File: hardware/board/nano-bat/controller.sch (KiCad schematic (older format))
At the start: 24 parts

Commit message: Adding larger microcontroller
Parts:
- removed U?: STM32L452CEUx, Package_DFN_QFN:QFN-48-1EP_7x7mm_P0.5mm_EP5.6x5.6mm, symbol MCU_ST_STM32L4:STM32L452CEUx
- added C?: .1u, symbol Device:C
- added D?: LED, symbol Device:LED
- added J?: Conn_01x10, symbol Connector_Generic:Conn_01x10
- added R?: R_US, symbol Device:R_US
- added R?: 1k, symbol Device:R_US
- added R? (x2): 10k, symbol Device:R_US
- added SW?: SW_Push, symbol Switch:SW_Push
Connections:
- net labels added: BTN1, BTN2, BTN3, BTN4, PB5, PD2, SPI2_MISO, SPI2_MOSI, SPI2_NSS, SPI2_SCK, SWCLK
- net labels removed: SWDCLK
- wire segments 191 -> 219
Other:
- moved on the sheet: C?, FB?, J?, R?, SW?, U?

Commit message: Adding WIP before reverting
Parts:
- removed U?: STM32L452RETx, Package_QFP:LQFP-64_10x10mm_P0.5mm, symbol MCU_ST_STM32L4:STM32L452RETx
- added U?: STM32L452CEUx, Package_DFN_QFN:QFN-48-1EP_7x7mm_P0.5mm_EP5.6x5.6mm, symbol MCU_ST_STM32L4:STM32L452CEUx
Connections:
- net labels added: CC_SCL, CC_SDA, CC_~AL~CC, TFT_BL_CNTRL
- net labels removed: CC_POL, CC_~INT, CC_~SHDN, DB0, DB1, DB2, DB3, DB4, DB5, DB6, DB7, LCD-TFT_DB, LCD_EN, LCD_RS, LCD_R~W, TFT_RD, TFT_RGB_DOTCLK, TFT_RGB_EN, TFT_RGB_HSYNC, TFT_RGB_VSYNC, TFT_WR
- wire segments 219 -> 192
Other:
- moved on the sheet: C?, FB?, R?

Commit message: Adding complete schematic
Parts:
- removed R? (x2): 10k, symbol Device:R_US
- added D?: LED, symbol Device:LED
- added R?: 1k, symbol Device:R_US
- R? (x5): value R_US -> 10k
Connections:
- net labels added: +2V8, I2C1_SCL, I2C1_SDA, PA2, PA8, TFT_D~CX
- net labels removed: +3.3V, PB5, PD2, Vsoc
- wire segments 192 -> 203
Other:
- moved on the sheet: C?, D?, FB?, J?, R?, SW?, U?

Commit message: Adding first-pass revisions and annotations, part selection
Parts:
- removed C? (x5): .1u, symbol Device:C
- removed C?: 4.7u, symbol Device:C
- removed C?: 1u, symbol Device:C
- removed FB?: Ferrite_Bead_Small, symbol Device:Ferrite_Bead_Small
- removed J?: Conn_01x10, symbol Connector_Generic:Conn_01x10
- removed R? (x7): 10k, symbol Device:R_US
- removed R? (x2): 1k, symbol Device:R_US
- removed SW? (x3): SW_Push, symbol Switch:SW_Push
- added C301, C302, C303, C304, C305, C308, C309, C310, C311: 0.1u, Capacitor_SMD:C_0603_1608Metric, symbol Device:C
- added C307: 1u, Capacitor_SMD:C_0603_1608Metric, symbol Device:C
- added C312: 4.7u, Capacitor_SMD:C_0603_1608Metric, symbol Device:C
- added FB302: Ferrite_Bead_Small, Resistor_SMD:R_0603_1608Metric, symbol Device:Ferrite_Bead_Small
- added J303: Conn_01x10, Connector_PinHeader_2.54mm:PinHeader_1x10_P2.54mm_Vertical, symbol Connector_Generic:Conn_01x10
- added R302, R304, R306, R308, R309, R311: 1k, Resistor_SMD:R_0603_1608Metric, symbol Device:R_US
- added R303, R305, R307, R310, R312, R313, R314: 10k, Resistor_SMD:R_0603_1608Metric, symbol Device:R_US
- added SW302, SW303, SW304: SW_Push, footprints:SW_B3FS-1010P, symbol Switch:SW_Push
- C306: renamed from C?; footprint (none) -> Capacitor_SMD:C_0603_1608Metric; Part (none) -> 399-7842-1-ND
- D301: renamed from D?; value LED -> BLU; footprint (none) -> LED_SMD:LED_0805_2012Metric; Part (none) -> 160-1645-1-ND
- D302: renamed from D?; value LED -> RED; footprint (none) -> LED_SMD:LED_0805_2012Metric; Part (none) -> 475-1278-1-ND
- FB301: renamed from FB?; footprint (none) -> Resistor_SMD:R_0603_1608Metric; Part (none) -> 587-1923-1-ND
- J301: renamed from J?; footprint (none) -> Connector_PinHeader_1.27mm:PinHeader_2x05_P1.27mm_Vertical_SMD; Part (none) -> SAM8796-ND
- J302: renamed from J?; footprint (none) -> Connector_PinHeader_2.54mm:PinHeader_1x10_P2.54mm_Vertical; Part (none) -> 609-3301-ND
- R301: renamed from R?; footprint (none) -> Resistor_SMD:R_0603_1608Metric; Part (none) -> 311-10KGRCT-ND
- SW301: renamed from SW?; footprint (none) -> footprints:SW_B3FS-1010P; Part (none) -> SW1440CT-ND
- U301: renamed from U?; Part (none) -> 497-6357-5-ND
- U302: renamed from U?; Part (none) -> 497-17218-ND
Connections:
- net +2V8: now also C308.1, C309.1, C310.1, C311.1, C312.1, FB302.2, J303.2 (Pin_2), J303.9 (Pin_9), R303.1, R305.1, R307.1, R309.1, R310.1, R311.1, R312.1, R313.1, R314.1
- net BTN1: now also C301.1, R302.1; no longer SW301.1
- net BTN2: now also C302.1, R303.2, R304.1
- net BTN3: now also C303.1, R305.2, R306.1
- net BTN4: now also C304.1, R307.2, R308.1
- net GND: now also C301.2, C302.2, C303.2, C304.2, C305.1, C308.2, C309.2, C310.2, C311.2, C312.2, J303.1 (Pin_1), J303.10 (Pin_10), SW302.2, SW303.2, SW304.2
- net GNDREF: now also C307.2
- net PA8: now also J303.3 (Pin_3)
- net SPI1_NSS: now also R313.2
- net TFT_MISO: now also J303.6 (Pin_6), J303.7 (Pin_7)
- net TFT_SCK: now also J303.5 (Pin_5)
- net TFT_~CS: now also J303.8 (Pin_8)
- net VDDA: now also C307.1, FB302.1
- net ~RST: now also C305.2, R314.2
- net at U301.3 (~W): now also R310.2
- net at U301.7 (~HOLD): now also R312.2
- net PB8: now reaches U302.45 (PB8)
- net PB8: now also J303.4 (Pin_4)
- net at D302.2 (A): now also R311.2
- net at D301.2 (A): now also R309.2
- net PA2 renamed Pen
- new net: R302.2, SW301.1
- new net: R304.2, SW302.1
- new net: R306.2, SW303.1
- new net: R308.2, SW304.1
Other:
- moved on the sheet: D301, D302, R301, SW301, U301, U302

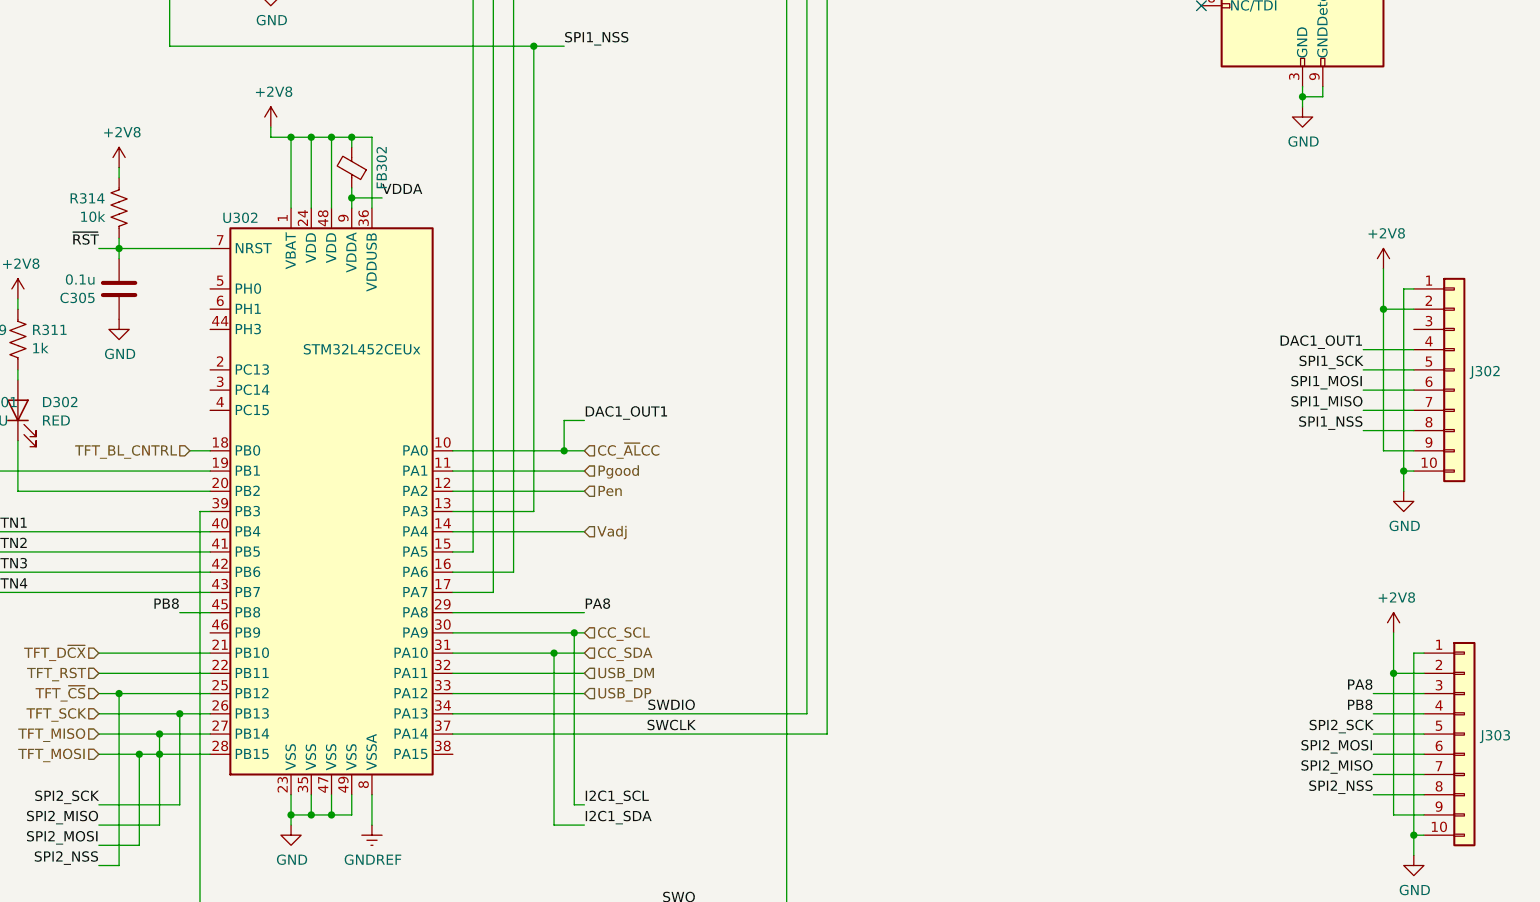
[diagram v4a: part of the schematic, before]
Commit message: Adding 3D models, reorg, minor schematic fixes
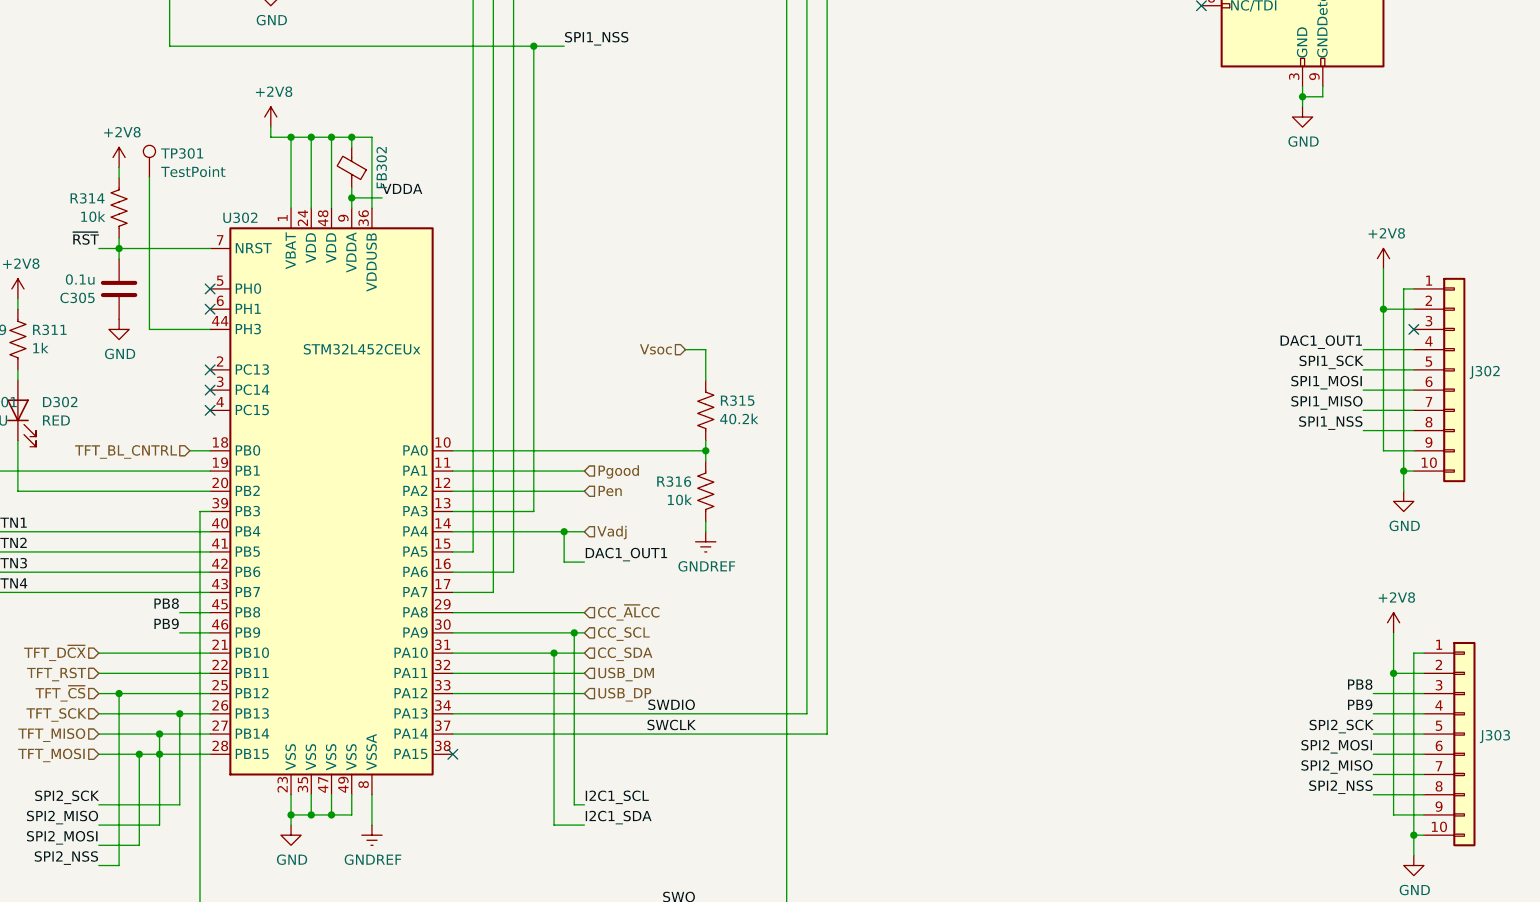
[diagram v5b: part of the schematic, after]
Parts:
- added R315: 40.2k, Resistor_SMD:R_0603_1608Metric, symbol Device:R_US
- added R316: 10k, Resistor_SMD:R_0603_1608Metric, symbol Device:R_US
- added TP301: TestPoint, TestPoint:TestPoint_Plated_Hole_D2.0mm, symbol Connector:TestPoint
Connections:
- net CC_~AL~CC: now also U302.29 (PA8); no longer J302.4 (Pin_4), U302.10 (PA0)
- net GNDREF: now also R316.2
- net PB8: now also J303.3 (Pin_3); no longer J303.4 (Pin_4)
- net Vadj: now also J302.4 (Pin_4)
- net at U302.44 (PH3): now also TP301.1
- net PB9: now reaches U302.46 (PB9)
- net PB9: now also J303.4 (Pin_4)
- removed net PA8: J303.3 (Pin_3), U302.29 (PA8)
- new net: R315.2, R316.1, U302.10 (PA0)
- new net Vsoc: R315.1
- no-connect marks 1 -> 8
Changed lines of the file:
@@
 	9800 2300 9800 2350
 NoConn ~ 9300 1850
-Text HLabel 6250 4450 2    50   Input ~ 0
-Vadj
 Text Label 10100 3550 2    50   ~ 0
 DAC1_OUT1
@@
 Text HLabel 6250 4950 2    50   Input ~ 0
 CC_SCL
-Text HLabel 6250 4050 2    50   Input ~ 0
-CC_~AL~CC
 $Comp
 L MCU_ST_STM32L4:STM32L452CEUx U302
@@
 	6150 1400 5800 1400
 Wire Wire Line
-	5600 4450 6250 4450
+	5600 4450 6150 4450
 Connection ~ 5700 1300
 Connection ~ 5800 1400
@@
 	6150 2050 6000 2050
 Connection ~ 6000 2050
-Wire Wire Line
-	6150 4050 5600 4050
-Wire Wire Line
-	6250 4050 6150 4050
-Connection ~ 6150 4050
-Wire Wire Line
-	6150 3900 6150 4050
-Wire Wire Line
-	6250 3900 6150 3900
-Text Label 6250 3900 0    50   ~ 0
+Text Label 6250 4600 0    50   ~ 0
 DAC1_OUT1
 Text Label 3500 4450 2    50   ~ 0
@@
 Wire Wire Line
 	3150 4000 3150 4150
-Text Label 6250 4850 0    50   ~ 0
-PA8
-Wire Wire Line
-	5600 4850 6250 4850
 Text Label 4250 4850 2    50   ~ 0
 PB8
 Text Label 10150 5250 2    50   ~ 0
-PA8
-Text Label 10150 5350 2    50   ~ 0
 PB8
+Text Label 10150 5350 2    50   ~ 0
+PB9
 Wire Wire Line
 	10150 5350 10400 5350
@@
 	1    0    0    -1
 $EndComp
+Text HLabel 6250 4450 2    50   Input ~ 0
+Vadj
+Text HLabel 6250 4850 2    50   Input ~ 0
+CC_~AL~CC
+Wire Wire Line
+	6250 4600 6150 4600
+Wire Wire Line
+	6150 4600 6150 4450
+Connection ~ 6150 4450
+Wire Wire Line
+	6150 4450 6250 4450
+$Comp
+L Device:R_US R315
+U 1 1 5E695531
+P 6850 3850
+F 0 "R315" H 6918 3896 50  0000 L CNN
+F 1 "40.2k" H 6918 3805 50  0000 L CNN
+F 2 "Resistor_SMD:R_0603_1608Metric" V 6890 3840 50  0001 C CNN
+F 3 "~" H 6850 3850 50  0001 C CNN
+F 4 "RR08P40.2KDCT-ND" H 6850 3850 50  0001 C CNN "Part"
+	1    6850 3850
+	1    0    0    -1
+$EndComp
+Text HLabel 6750 3550 0    50   Input ~ 0
+Vsoc
+$Comp
+L power:GNDREF #PWR0168
+U 1 1 5E6A65E6
+P 6850 4450
+F 0 "#PWR0168" H 6850 4200 50  0001 C CNN
+F 1 "GNDREF" H 6855 4277 50  0000 C CNN
+F 2 "" H 6850 4450 50  0001 C CNN
+F 3 "" H 6850 4450 50  0001 C CNN
+	1    6850 4450
+	1    0    0    -1
+$EndComp
+Wire Wire Line
+	6850 4450 6850 4400
+Wire Wire Line
+	6750 3550 6850 3550
+Wire Wire Line
+	6850 3550 6850 3700
+Wire Wire Line
+	6850 4100 6850 4050
+Wire Wire Line
+	5600 4050 6850 4050
+Connection ~ 6850 4050
+Wire Wire Line
+	6850 4050 6850 4000
+Wire Wire Line
+	6250 4850 5600 4850
+Text Label 4250 4950 2    50   ~ 0
+PB9
+Wire Wire Line
+	4250 4950 4400 4950
+$Comp
+L Device:R_US R316
+U 1 1 5E72ACDB
+P 6850 4250
+F 0 "R316" H 6918 4296 50  0000 L CNN
+F 1 "10k" H 6918 4205 50  0000 L CNN
+F 2 "Resistor_SMD:R_0603_1608Metric" V 6890 4240 50  0001 C CNN
+F 3 "~" H 6850 4250 50  0001 C CNN
+F 4 "311-10KGRCT-ND" H 6850 4250 50  0001 C CNN "Part"
+	1    6850 4250
+	-1   0    0    -1
+$EndComp
+NoConn ~ 10350 3450
+$Comp
+L Connector:TestPoint TP301
+U 1 1 5E73C90B
+P 4100 2700
+F 0 "TP301" H 4158 2818 50  0000 L CNN
+F 1 "TestPoint" H 4158 2727 50  0000 L CNN
+F 2 "TestPoint:TestPoint_Plated_Hole_D2.0mm" H 4300 2700 50  0001 C CNN
+F 3 "~" H 4300 2700 50  0001 C CNN
+	1    4100 2700
+	1    0    0    -1
+$EndComp
+Wire Wire Line
+	4400 3450 4100 3450
+Wire Wire Line
+	4100 3450 4100 2700
+NoConn ~ 5600 5550
+NoConn ~ 4400 3350
+NoConn ~ 4400 3250
+NoConn ~ 4400 3650
+NoConn ~ 4400 3750
+NoConn ~ 4400 3850
 $EndSCHEMATC

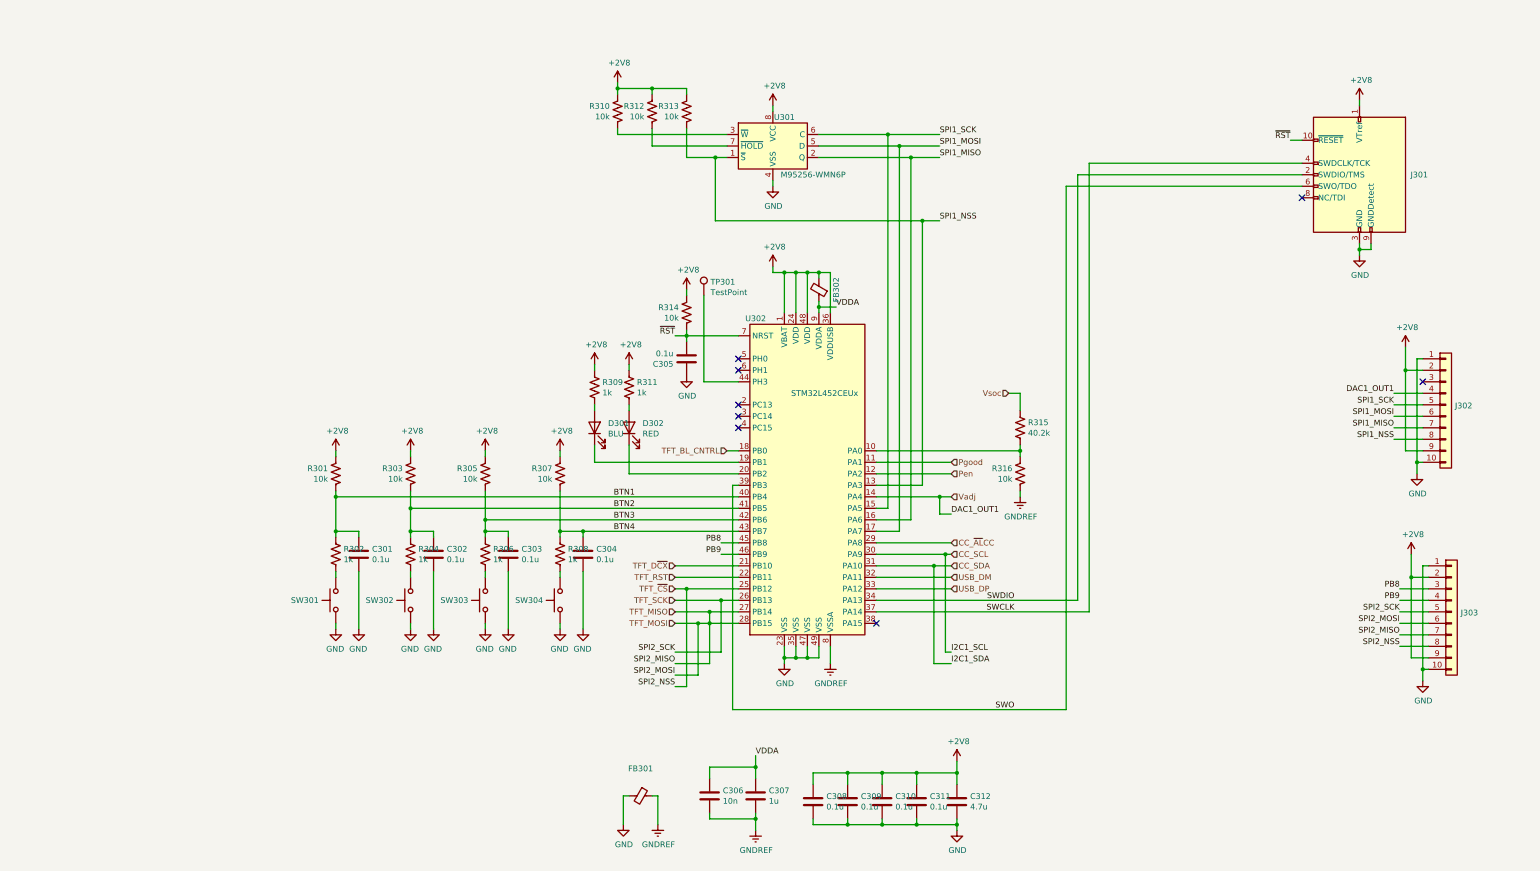
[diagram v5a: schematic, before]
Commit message: Adding docs to schematic
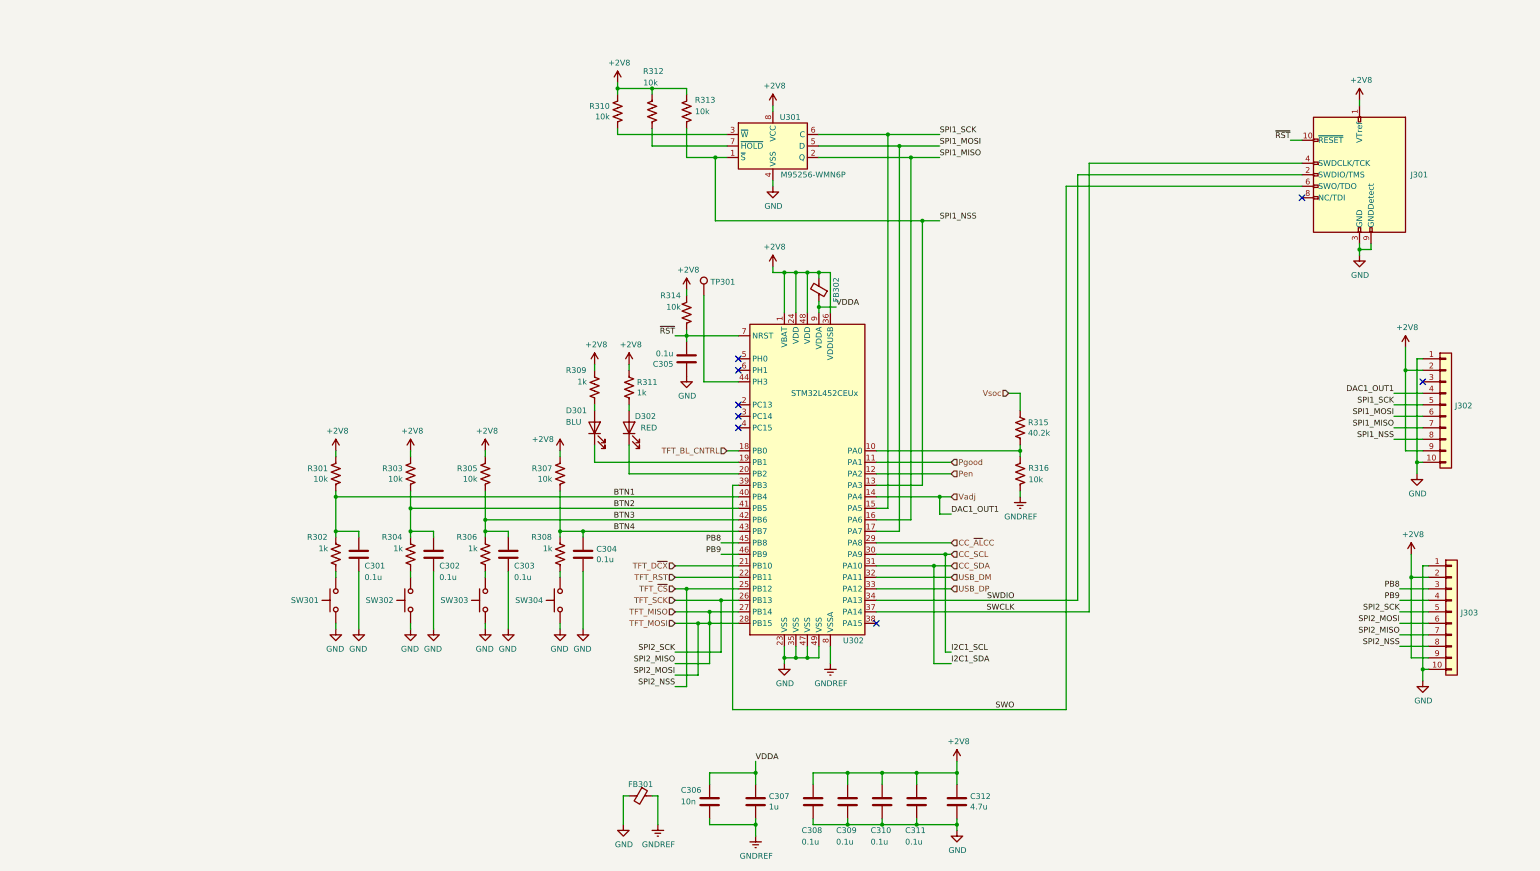
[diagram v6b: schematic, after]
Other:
- moved on the sheet: C306, C307

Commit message: Adding 0.1.0 of board spin
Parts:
- removed D301: BLU, LED_SMD:LED_0805_2012Metric, symbol Device:LED
- removed R309: 1k, Resistor_SMD:R_0603_1608Metric, symbol Device:R_US
- added TP302, TP303, TP304, TP305, TP306: TestPoint, TestPoint:TestPoint_Pad_D1.0mm, symbol Connector:TestPoint
- TP301: footprint TestPoint:TestPoint_Plated_Hole_D2.0mm -> TestPoint:TestPoint_THTPad_D1.0mm_Drill0.5mm
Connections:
- net +2V8: now also J302.3 (Pin_3), J302.4 (Pin_4); no longer J302.2 (Pin_2), J302.9 (Pin_9), J303.2 (Pin_2), J303.9 (Pin_9)
- net BTN1: now also TP302.1
- net BTN2: now also TP303.1
- net BTN3: now also TP304.1
- net BTN4: now also TP305.1
- net CC_SCL: now also J303.9 (Pin_9)
- net CC_SDA: now also J303.8 (Pin_8)
- net CC_~AL~CC: now also TP306.1
- net PB8: now also J302.2 (Pin_2); no longer J303.3 (Pin_3)
- net PB9: now also J303.7 (Pin_7); no longer J303.4 (Pin_4)
- net SPI1_MISO: now also J303.5 (Pin_5); no longer J302.7 (Pin_7)
- net SPI1_MOSI: now also J303.6 (Pin_6); no longer J302.6 (Pin_6)
- net SPI1_NSS: now also J303.2 (Pin_2); no longer J302.8 (Pin_8)
- net SPI1_SCK: now also J303.3 (Pin_3); no longer J302.5 (Pin_5)
- net TFT_D~CX: now also J302.6 (Pin_6)
- net TFT_MISO: now also J302.9 (Pin_9); no longer J303.6 (Pin_6), J303.7 (Pin_7), U302.28 (PB15)
- net TFT_SCK: now also J302.7 (Pin_7); no longer J303.5 (Pin_5)
- net TFT_~CS: now also J302.5 (Pin_5); no longer J303.8 (Pin_8)
- net Vadj: now also J303.4 (Pin_4); no longer J302.4 (Pin_4)
- net CC_~500mA: now reaches U302.19 (PB1)
- net CC_~50mA: now reaches U302.38 (PA15)
- net Pgood renamed CC_~5mA
- new net TFT_MOSI: J302.8 (Pin_8), U302.28 (PB15)
- no-connect marks 8 -> 6
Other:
- moved on the sheet: J302, J303
